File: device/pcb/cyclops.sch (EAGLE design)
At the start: 180 parts, among them Q1 SSM3K324, Q2 SSM3K324, Q3 SSM3K324, Q4 IRF510, U1 MCP4921, U10 ADG1201, U11 THS4281, U12 MAX4564, U13 ZXTD, U14 ZXTD, U15 OPA1664, U2 LT1931, U3 LT1764A, U31 TPS62153, U4 BD00FC0WEFJ, U5 TPS72325, U6 LT1711, U7 TLV3701, U8 ADR03, U9 LT1880

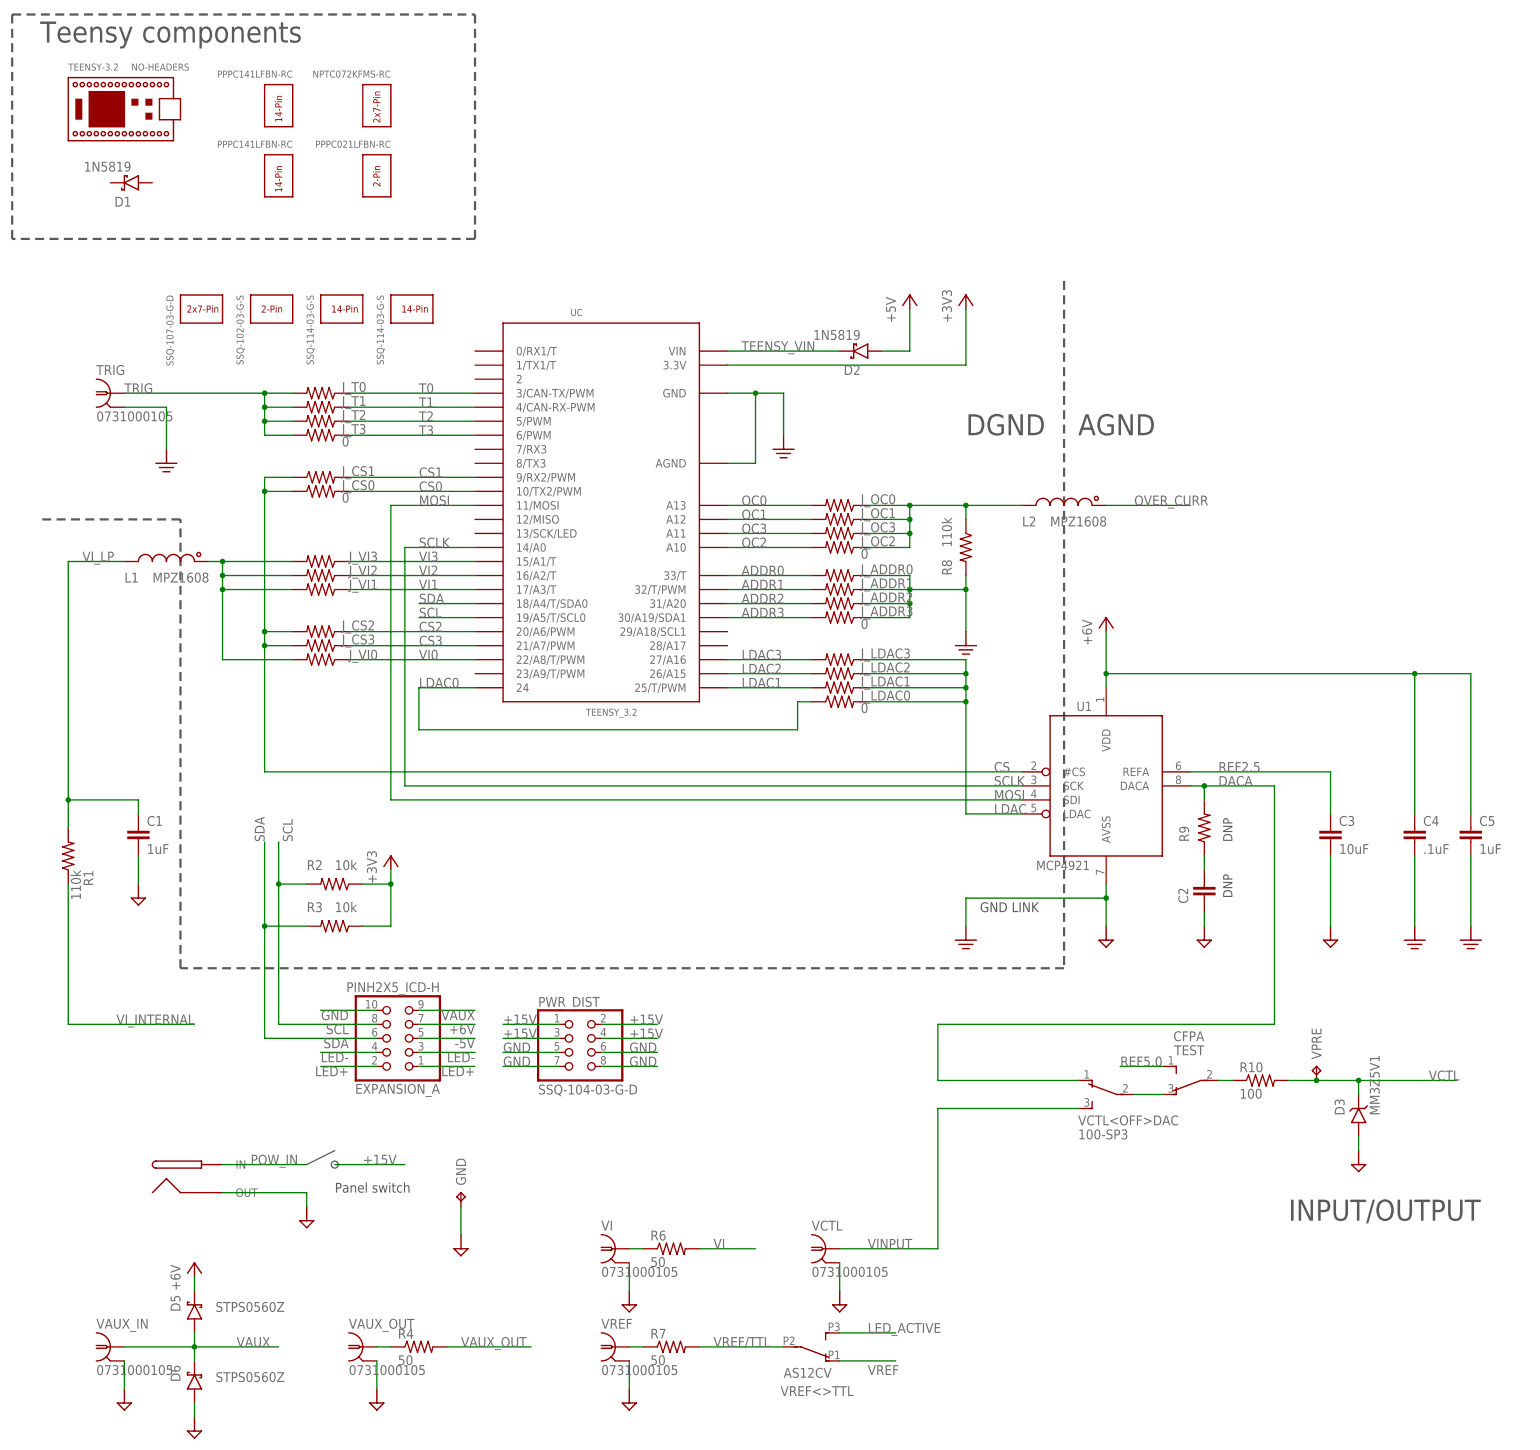
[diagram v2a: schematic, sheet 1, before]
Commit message: Fixed a couple circuit bugs found during prototype build.
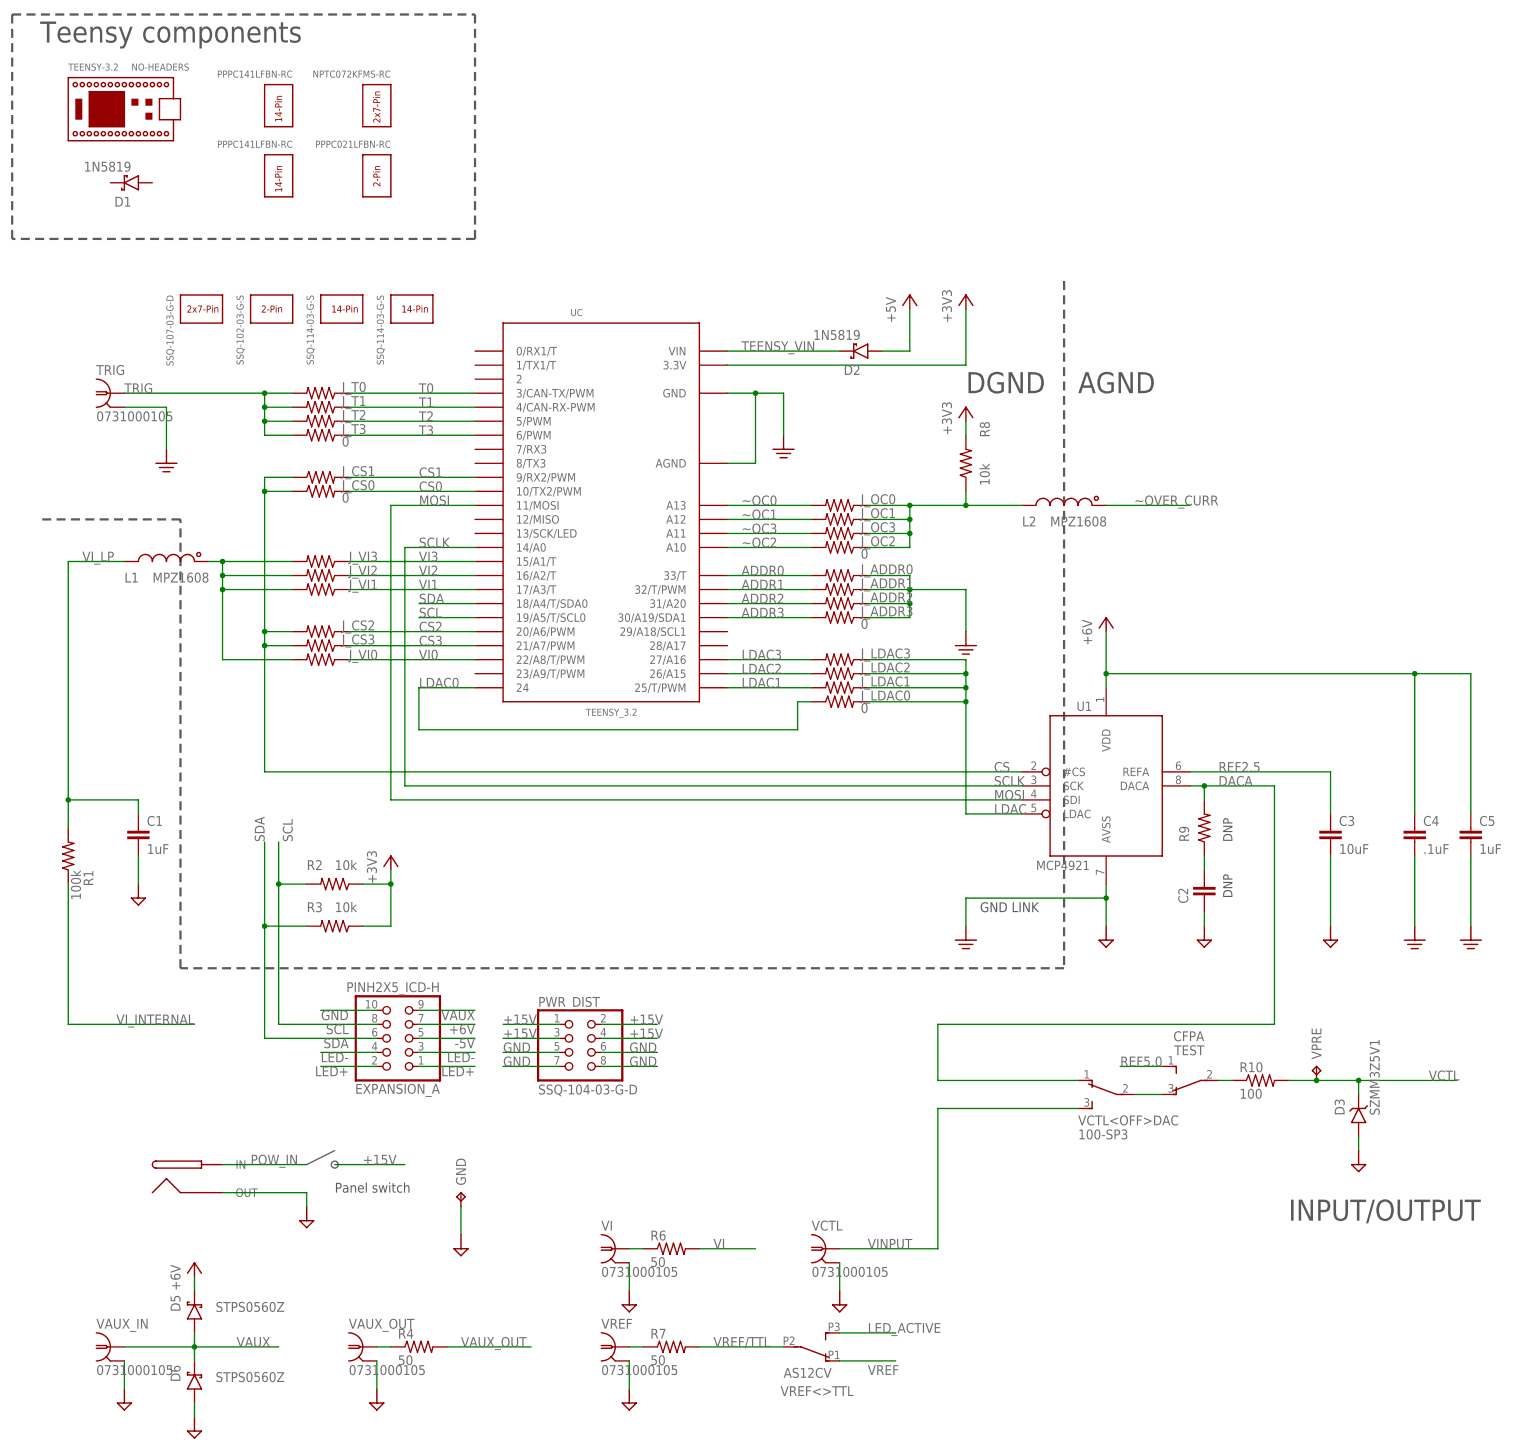
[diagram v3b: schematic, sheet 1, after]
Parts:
- D3: value MM3Z5V1 -> SZMM3Z5V1
- R1: value 110k -> 100k
- R8: value 110k -> 10k
- U10: value ADG1201 -> ADG1202
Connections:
- net OC0 renamed ~OC0
- net OC1 renamed ~OC1
- net OC2 renamed ~OC2
- net OC3 renamed ~OC3
- new net ~OVER_CURR: L2.1
- net +3V3: now also R8.2
- net -2.5V: no longer C15.2
- net GND: now also C15.2; no longer R8.2
- net OVER_CURR: no longer L2.1
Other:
- moved on the sheet: C15, R8
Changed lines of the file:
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@@
 <part name="J_VI1" library="jonnew" deviceset="R" device="_0402" value="0"/>
 <part name="J_VI0" library="jonnew" deviceset="R" device="_0402" value="0"/>
-<part name="R1" library="cyclops" deviceset="R" device="_0603" value="110k"/>
+<part name="R1" library="cyclops" deviceset="R" device="_0603" value="100k"/>
 <part name="C1" library="cyclops" deviceset="C" device="_0805" value="1uF"/>
 <part name="U$50" library="cyclops" deviceset="GND2" device=""/>
@@
 <part name="SUPPLY14" library="cyclops" deviceset="+12V" device=""/>
 <part name="R10" library="jonnew" deviceset="R" device="_0603" value="100"/>
-<part name="D3" library="cyclops" deviceset="Z-DIODE" device="_SOD-323" value="MM3Z5V1"/>
+<part name="D3" library="cyclops" deviceset="Z-DIODE" device="_SOD-323" value="SZMM3Z5V1"/>
 <part name="U$21" library="cyclops" deviceset="GND2" device=""/>
 <part name="R40" library="cyclops" deviceset="R" device="_0603" value="1k"/>
@@
 <part name="U$61" library="cyclops" deviceset="GND2" device=""/>
 <part name="P-7" library="cyclops" deviceset="-5V" device="" value="-1.25V"/>
-<part name="R8" library="cyclops" deviceset="R" device="_0603" value="110k"/>
+<part name="R8" library="cyclops" deviceset="R" device="_0603" value="10k"/>
 <part name="U$62" library="cyclops" deviceset="GND1" device=""/>
 <part name="R28" library="cyclops" deviceset="R" device="_0603" value="1k"/>
@@
 <part name="P+1" library="jonnew" deviceset="+5V" device="" value="+6V"/>
 <part name="P+5" library="jonnew" deviceset="+5V" device="" value="+6V"/>
-<part name="U10" library="jonnew" deviceset="SPST_IC" device="_SOT23-6" value="ADG1201"/>
+<part name="U10" library="jonnew" deviceset="SPST_IC" device="_SOT23-6" value="ADG1202"/>
 <part name="P+9" library="jonnew" deviceset="+5V" device="" value="+6V"/>
 <part name="P+10" library="jonnew" deviceset="+5V" device="" value="+6V"/>
@@
 <part name="C40" library="cyclops" deviceset="C" device="_1210" value="22uF"/>
 <part name="U$80" library="jonnew" deviceset="TEENSY-2-PIN-HEADER" device="" value="PPPC021LFBN-RC"/>
+<part name="P+20" library="cyclops" deviceset="+5V" device="" value="+3V3"/>
 </parts>
 <sheets>
@@
 <wire x1="177.8" y1="142.24" x2="177.8" y2="17.78" width="0.4064" layer="97" style="shortdash"/>
 <wire x1="177.8" y1="17.78" x2="17.78" y2="17.78" width="0.4064" layer="97" style="shortdash"/>
-<text x="180.34" y="114.3" size="3.81" layer="97">AGND</text>
-<text x="160.02" y="114.3" size="3.81" layer="97">DGND</text>
+<text x="180.34" y="121.92" size="3.81" layer="97">AGND</text>
+<text x="160.02" y="121.92" size="3.81" layer="97">DGND</text>
 <wire x1="17.78" y1="17.78" x2="17.78" y2="99.06" width="0.4064" layer="97" style="shortdash"/>
 <wire x1="17.78" y1="99.06" x2="-7.62" y2="99.06" width="0.4064" layer="97" style="shortdash"/>
@@
 <instance part="U$21" gate="G$1" x="231.14" y="-17.78"/>
 <instance part="VPRE" gate="G$1" x="223.52" y="0"/>
-<instance part="R8" gate="R" x="160.02" y="93.98" smashed="yes" rot="R270">
-<attribute name="NAME" x="157.48" y="88.9" size="1.778" layer="95" rot="R90"/>
-<attribute name="VALUE" x="157.48" y="93.98" size="1.778" layer="96" rot="R90"/>
+<instance part="R8" gate="R" x="160.02" y="109.22" smashed="yes" rot="R90">
+<attribute name="NAME" x="162.56" y="116.84" size="1.778" layer="95" rot="R270"/>
+<attribute name="VALUE" x="162.56" y="109.22" size="1.778" layer="96" rot="R270"/>
 </instance>
 <instance part="U$62" gate="G$1" x="160.02" y="76.2"/>
@@
 <instance part="U$79" gate="G$1" x="68.58" y="-33.02"/>
 <instance part="U$80" gate="G$1" x="50.8" y="165.1" rot="R270"/>
+<instance part="P+20" gate="1" x="160.02" y="119.38"/>
 </instances>
 <busses>
@@
 </segment>
 <segment>
-<pinref part="R8" gate="R" pin="2"/>
 <wire x1="160.02" y1="78.74" x2="160.02" y2="86.36" width="0.1524" layer="91"/>
 <pinref part="J_ADDR3" gate="R" pin="1"/>
-<wire x1="160.02" y1="86.36" x2="160.02" y2="88.9" width="0.1524" layer="91"/>
 <wire x1="142.24" y1="81.28" x2="149.86" y2="81.28" width="0.1524" layer="91"/>
 <wire x1="149.86" y1="81.28" x2="149.86" y2="83.82" width="0.1524" layer="91"/>
@@
 <junction x="149.86" y="83.82"/>
 <wire x1="149.86" y1="86.36" x2="160.02" y2="86.36" width="0.1524" layer="91"/>
-<junction x="160.02" y="86.36"/>
 </segment>
 <segment>
@@
 <wire x1="116.84" y1="127" x2="160.02" y2="127" width="0.1524" layer="91"/>
 <wire x1="160.02" y1="127" x2="160.02" y2="137.16" width="0.1524" layer="91"/>
+</segment>
+<segment>
+<pinref part="R8" gate="R" pin="2"/>
+<wire x1="160.02" y1="116.84" x2="160.02" y2="114.3" width="0.1524" layer="91"/>
 </segment>
 </net>
@@
 </segment>
 </net>
-<net name="OVER_CURR" class="0">
-<segment>
-<pinref part="L2" gate="L" pin="1"/>
-<wire x1="185.42" y1="101.6" x2="200.66" y2="101.6" width="0.1524" layer="91"/>
-<label x="190.5" y="101.6" size="1.778" layer="95"/>
-</segment>
-</net>
-<net name="OC3" class="0">
+<net name="~OC3" class="0">
 <segment>
 <pinref part="J_OC3" gate="R" pin="2"/>
@@
 </segment>
 </net>
-<net name="OC1" class="0">
+<net name="~OC1" class="0">
 <segment>
 <pinref part="J_OC1" gate="R" pin="2"/>
@@
 <wire x1="160.02" y1="101.6" x2="170.18" y2="101.6" width="0.1524" layer="91"/>
 <pinref part="R8" gate="R" pin="1"/>
-<wire x1="160.02" y1="99.06" x2="160.02" y2="101.6" width="0.1524" layer="91"/>
+<wire x1="160.02" y1="104.14" x2="160.02" y2="101.6" width="0.1524" layer="91"/>
 <junction x="160.02" y="101.6"/>
 <pinref part="J_OC1" gate="R" pin="1"/>
@@
 </segment>
 </net>
-<net name="OC2" class="0">
+<net name="~OC2" class="0">
 <segment>
 <pinref part="J_OC2" gate="R" pin="2"/>
@@
 </segment>
 </net>
-<net name="OC0" class="0">
+<net name="~OC0" class="0">
 <segment>
 <pinref part="J_OC0" gate="R" pin="2"/>
@@
 <label x="60.96" y="78.74" size="1.778" layer="95"/>
 <pinref part="UC" gate="G$1" pin="20/A6/PWM"/>
+</segment>
+</net>
+<net name="~OVER_CURR" class="0">
+<segment>
+<pinref part="L2" gate="L" pin="1"/>
+<wire x1="185.42" y1="101.6" x2="200.66" y2="101.6" width="0.1524" layer="91"/>
+<label x="190.5" y="101.6" size="1.778" layer="95"/>
 </segment>
 </net>
@@
 <instance part="L3" gate="G$2" x="-48.26" y="-88.9" rot="R270"/>
 <instance part="U$8" gate="G$1" x="-27.94" y="-142.24"/>
-<instance part="L4" gate="L" x="50.8" y="-96.52" smashed="yes" rot="R90">
-<attribute name="NAME" x="58.42" y="-95.25" size="1.778" layer="95" rot="R180"/>
-</instance>
+<instance part="L4" gate="L" x="50.8" y="-96.52" rot="R90"/>
 <instance part="C6" gate="C" x="-78.74" y="-111.76"/>
 <instance part="U3" gate="G$1" x="-38.1" y="38.1"/>
@@
 <instance part="+6V" gate="G$1" x="124.46" y="40.64"/>
 <instance part="U5" gate="G$1" x="96.52" y="-124.46" rot="MR180"/>
-<instance part="C15" gate="C" x="111.76" y="-124.46"/>
+<instance part="C15" gate="C" x="111.76" y="-111.76" rot="R180"/>
 <instance part="C13" gate="C" x="76.2" y="-111.76"/>
 <instance part="C16" gate="C" x="121.92" y="-111.76"/>
@@
 <wire x1="76.2" y1="-88.9" x2="96.52" y2="-88.9" width="0.1524" layer="91"/>
 <junction x="96.52" y="-88.9"/>
-<wire x1="96.52" y1="-88.9" x2="121.92" y2="-88.9" width="0.1524" layer="91"/>
+<wire x1="96.52" y1="-88.9" x2="111.76" y2="-88.9" width="0.1524" layer="91"/>
 <pinref part="C16" gate="C" pin="1"/>
+<wire x1="111.76" y1="-88.9" x2="121.92" y2="-88.9" width="0.1524" layer="91"/>
 <wire x1="121.92" y1="-88.9" x2="132.08" y2="-88.9" width="0.1524" layer="91"/>
 <wire x1="121.92" y1="-109.22" x2="121.92" y2="-88.9" width="0.1524" layer="91"/>
 <junction x="121.92" y="-88.9"/>
+<pinref part="C15" gate="C" pin="2"/>
+<wire x1="111.76" y1="-106.68" x2="111.76" y2="-88.9" width="0.1524" layer="91"/>
+<junction x="111.76" y="-88.9"/>
 </segment>
 <segment>
@@
 <pinref part="-2.5V" gate="G$1" pin="TP"/>
 <pinref part="U5" gate="G$1" pin="VO"/>
-<wire x1="109.22" y1="-132.08" x2="111.76" y2="-132.08" width="0.1524" layer="91"/>
 <junction x="134.62" y="-132.08"/>
-<pinref part="C15" gate="C" pin="2"/>
-<wire x1="111.76" y1="-132.08" x2="121.92" y2="-132.08" width="0.1524" layer="91"/>
+<wire x1="109.22" y1="-132.08" x2="121.92" y2="-132.08" width="0.1524" layer="91"/>
 <wire x1="121.92" y1="-132.08" x2="134.62" y2="-132.08" width="0.1524" layer="91"/>
-<wire x1="111.76" y1="-129.54" x2="111.76" y2="-132.08" width="0.1524" layer="91"/>
-<junction x="111.76" y="-132.08"/>
 <pinref part="C16" gate="C" pin="2"/>
 <wire x1="121.92" y1="-116.84" x2="121.92" y2="-132.08" width="0.1524" layer="91"/>
@@
 <pinref part="C15" gate="C" pin="1"/>
 <wire x1="109.22" y1="-121.92" x2="111.76" y2="-121.92" width="0.1524" layer="91"/>
-</segment>
-</net>
+<wire x1="111.76" y1="-121.92" x2="111.76" y2="-119.38" width="0.1524" layer="91"/>
+<wire x1="111.76" y1="-119.38" x2="111.76" y2="-114.3" width="0.1524" layer="91"/>
+</segment>
+</net>
